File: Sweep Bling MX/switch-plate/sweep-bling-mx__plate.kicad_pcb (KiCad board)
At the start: 2 copper layers, 111.6 x 95.2 mm, 26 parts, among them SW10 SW_Push, SW11 SW_Push, SW12 SW_Push, SW14 SW_Push, SW15 SW_Push, SW16 SW_Push, SW17 SW_Push, SW18 SW_Push, SW2 SW_Push, SW20 SW_Push, SW21 SW_Push, SW3 SW_Push, SW4 SW_Push, SW5 SW_Push, SW6 SW_Push, SW8 SW_Push, SW9 SW_Push

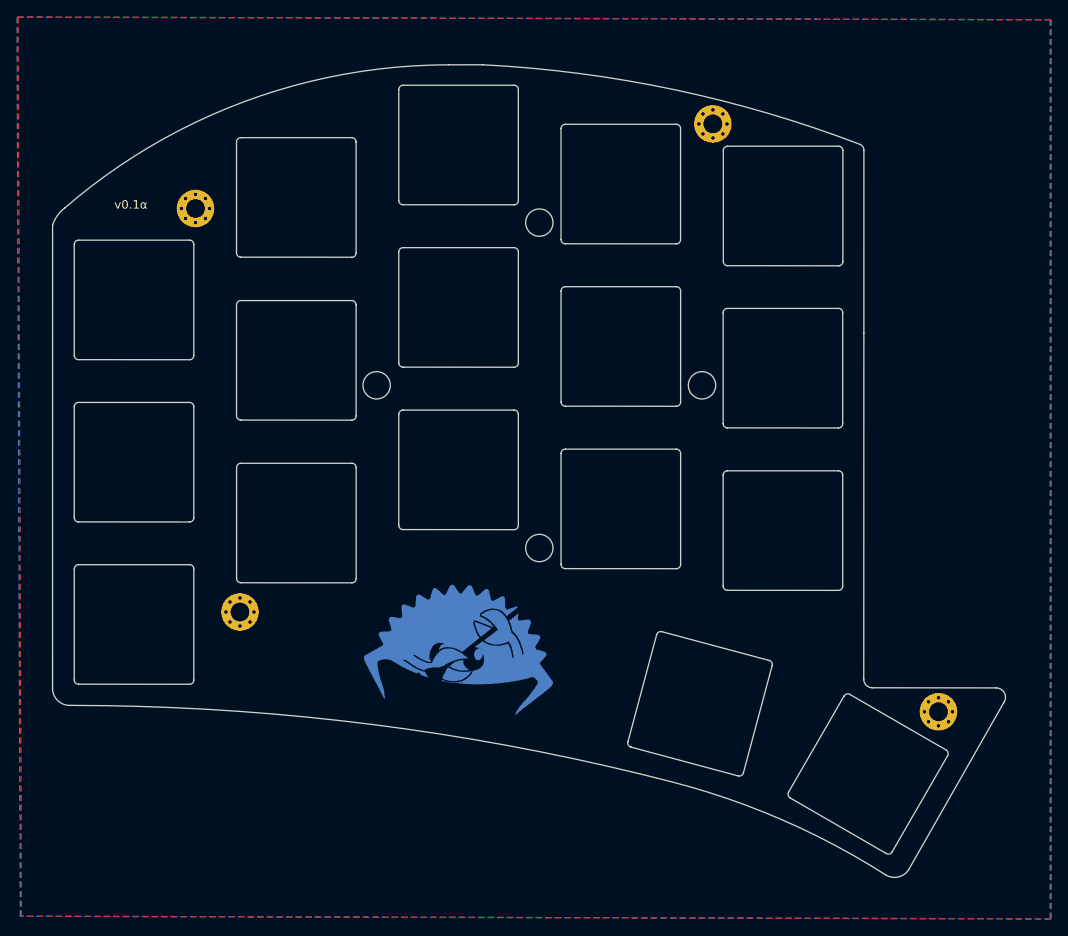
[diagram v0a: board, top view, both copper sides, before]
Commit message: Fix for issue#39
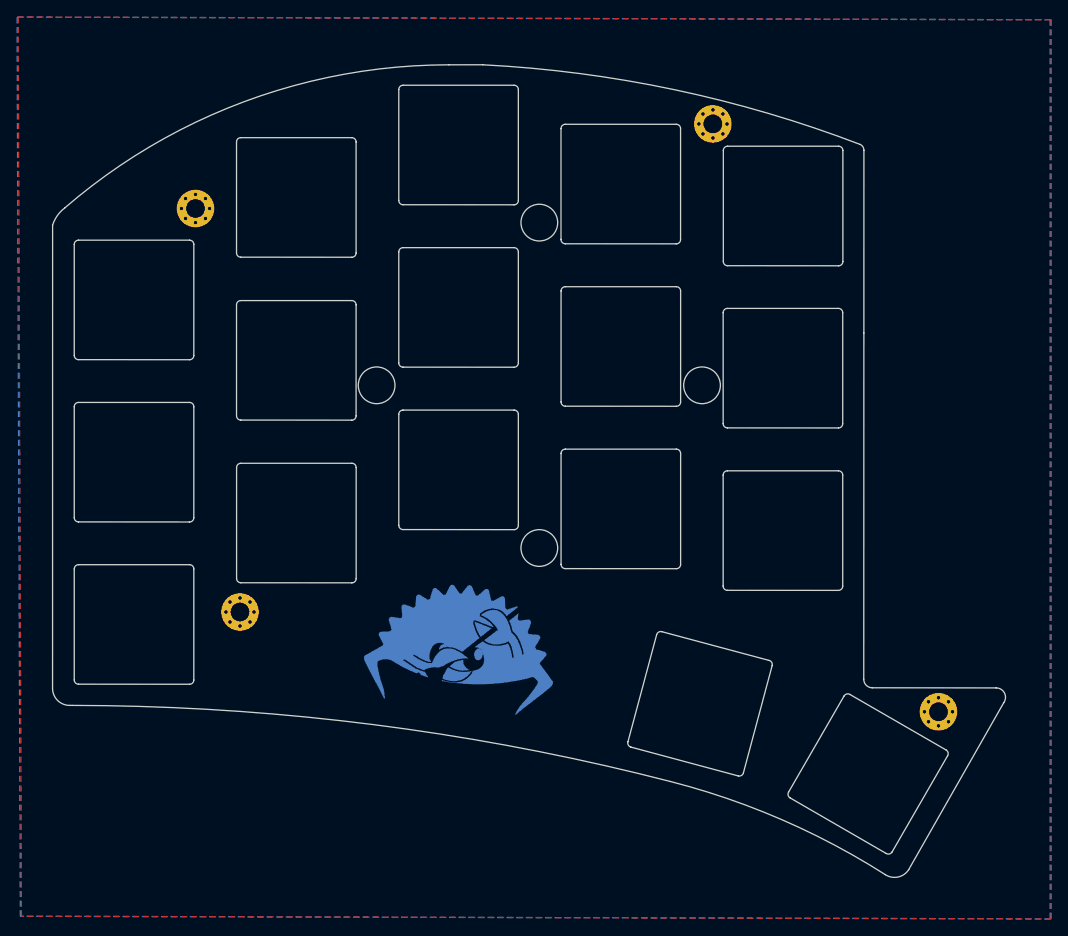
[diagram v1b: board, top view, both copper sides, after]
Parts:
- Puck1, Puck2, Puck3, Puck4: value MountingHole_3.2mm_M3 -> MountingHole_4.3mm_M4; footprint MountingHole:MountingHole_3.2mm_M3 -> MountingHole:MountingHole_4.3mm_M4
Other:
- net class Default removed
- board text removed: "v0.1α"
